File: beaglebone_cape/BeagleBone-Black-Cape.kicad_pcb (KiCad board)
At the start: 2 copper layers, 54.6 x 86.4 mm, 49 parts, among them J1 MC000052, J10 MOLEX_2031, J11 MOLEX_2021, J12 EBV-02-D, J2 MOLEX_2051, J3 MOLEX_2031, J4 MOLEX_2021, J5 MOLEX_2041, J6 MOLEX_2031, J7 MOLEX_2041, J8 MOLEX_2031, J9 MOLEX_2041, P1 BeagleBone_Black_Header, P2 BeagleBone_Black_Header, Q1 IRLB8721PBF, Q2 IRFML8244, U1 DIGIPOT_50K, U2 U_IC-HKB, U3 X_STEPPER, U4 Y_STEPPER, U5 Z_STEPPER

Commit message: finished layout of all PCBs
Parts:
- removed C1: 47nF, Capacitors_SMD:C_0805_HandSoldering
- removed C2, C6: 1uF, Capacitors_SMD:C_0805_HandSoldering
- removed C3: 0.1uF, Capacitors_SMD:C_0805_HandSoldering
- removed D5: 50V_1A, Diodes_SMD:D_SMA_Handsoldering
- removed J11, J4: MOLEX_2021, Connectors_Molex:Molex_KK-6410-02_02x2.54mm_Straight
- removed Q2: IRFML8244, TO_SOT_Packages_SMD:SOT-23
- removed R1, R2, R7: 10K, Resistors_SMD:R_0805_HandSoldering
- removed R3: 340K, Resistors_SMD:R_0805_HandSoldering
- removed TP1: TestPoint, Measurement_Points:Measurement_Point_Round-TH_Small
- removed U1: DIGIPOT_50K, Socket_BeagleBone_Black:TDFN-8-1EP
- removed U2: U_IC-HKB, Socket_BeagleBone_Black:ICHKB
- C4, C5, CP_1: footprint Capacitors_THT:CP_Radial_D6.3mm_P2.50mm -> Capacitor_THT:CP_Radial_D6.3mm_P2.50mm
- C7, C8, C9: footprint Capacitors_SMD:C_0805_HandSoldering -> Capacitor_SMD:C_0805_2012Metric_Pad1.15x1.40mm_HandSolder
- D1, D2, D3: footprint Diodes_SMD:D_SMA_Handsoldering -> Diode_SMD:D_SMA_Handsoldering
- D4: footprint TO_SOT_Packages_THT:TO-220-2_Vertical -> Package_TO_SOT_THT:TO-220-2_Vertical
- J10, J3, J6, J8: footprint Connectors_Molex:Molex_KK-6410-03_03x2.54mm_Straight -> Connector_Molex:Molex_KK-254_AE-6410-03A_1x03_P2.54mm_Vertical
- J12: footprint Connectors_Terminal_Blocks:TerminalBlock_bornier-2_P5.08mm -> TerminalBlock:TerminalBlock_bornier-2_P5.08mm
- J2: value MOLEX_2051 -> 10pinIDC; footprint Connectors_Molex:Molex_KK-6410-05_05x2.54mm_Straight -> Connector_IDC:IDC-Header_2x05_P2.54mm_Vertical
- J5, J7, J9: footprint Connectors_Molex:Molex_KK-6410-04_04x2.54mm_Straight -> Connector_Molex:Molex_KK-254_AE-6410-04A_1x04_P2.54mm_Vertical
- Q1: footprint TO_SOT_Packages_THT:TO-220-3_Vertical -> Package_TO_SOT_THT:TO-220-3_Vertical
- R4, R5, R6, R8: footprint Resistors_SMD:R_0805_HandSoldering -> Resistor_SMD:R_0805_2012Metric_Pad1.15x1.40mm_HandSolder
- moved J3 24.1 mm to (134.6, 65.0), turned to 90 degrees
- moved J2 17.5 mm to (124.3, 89.8), turned to 0 degrees
- moved J8 3.66 mm to (124.5, 80.8), turned to 90 degrees
- moved F2 2.07 mm to (152.1, 62.2)
- moved J6 1.11 mm to (134.6, 103.6)
- moved D4 0.94 mm to (159.9, 113.6)
- moved R5 0.42 mm to (129.3, 78.5), turned to 90 degrees
- moved Q1 0.28 mm to (150.5, 125.9)
- moved U5 0.23 mm to (148.6, 91.0)
- moved U3 0.18 mm to (132.7, 109.3)
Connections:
- J2 pad 1: +24V -> GND
- J2 pad 2: GND -> POLY_EN
- J2 pad 3: POLY_EN -> POLY_READY
- J2 pad 4: POLY_READY -> POLY_PWM
- J2 pad 5: POLY_PWM -> FAN_PWM
- J3 pad 1: +3V3 -> +12V
- J3 pad 2: PH_DIODE -> +5V
- P1 pad 11: Y_ENABLE -> Net-(P1-Pad11)
- P1 pad 18: Z_ENABLE -> Net-(P1-Pad18)
- P2 pad 12: X_ENABLE -> ENABLE
- U3 pad 1: X_ENABLE -> ENABLE
- U4 pad 1: Y_ENABLE -> ENABLE
- U5 pad 1: Z_ENABLE -> ENABLE
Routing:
- net GND: track 351.6 -> 205.6 mm
- net ENABLE: track 0.00 -> 137.4 mm
- net IC_HB_PWM2: track 111.6 -> 19.8 mm
- net FAN_PWM: track 33.0 -> 122.0 mm
- net X_ENABLE: track 69.3 -> 0.00 mm
- net IC_HB_PWM1: track 47.6 -> 14.1 mm
- net Z_ENABLE: track 33.0 -> 0.00 mm
- net +3V3: track 201.5 -> 169.8 mm
- net Net-(F2-Pad1): track 58.9 -> 29.7 mm
- net +5V: track 63.8 -> 85.7 mm
- net Y_ENABLE: track 13.6 -> 0.00 mm
- net POT_W: track 12.1 -> 0.00 mm
- net Net-(D5-Pad2): track 9.44 -> 0.00 mm
- net POLY_EN: track 20.7 -> 11.6 mm
- net SPIO_DI: track 122.9 -> 129.8 mm
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
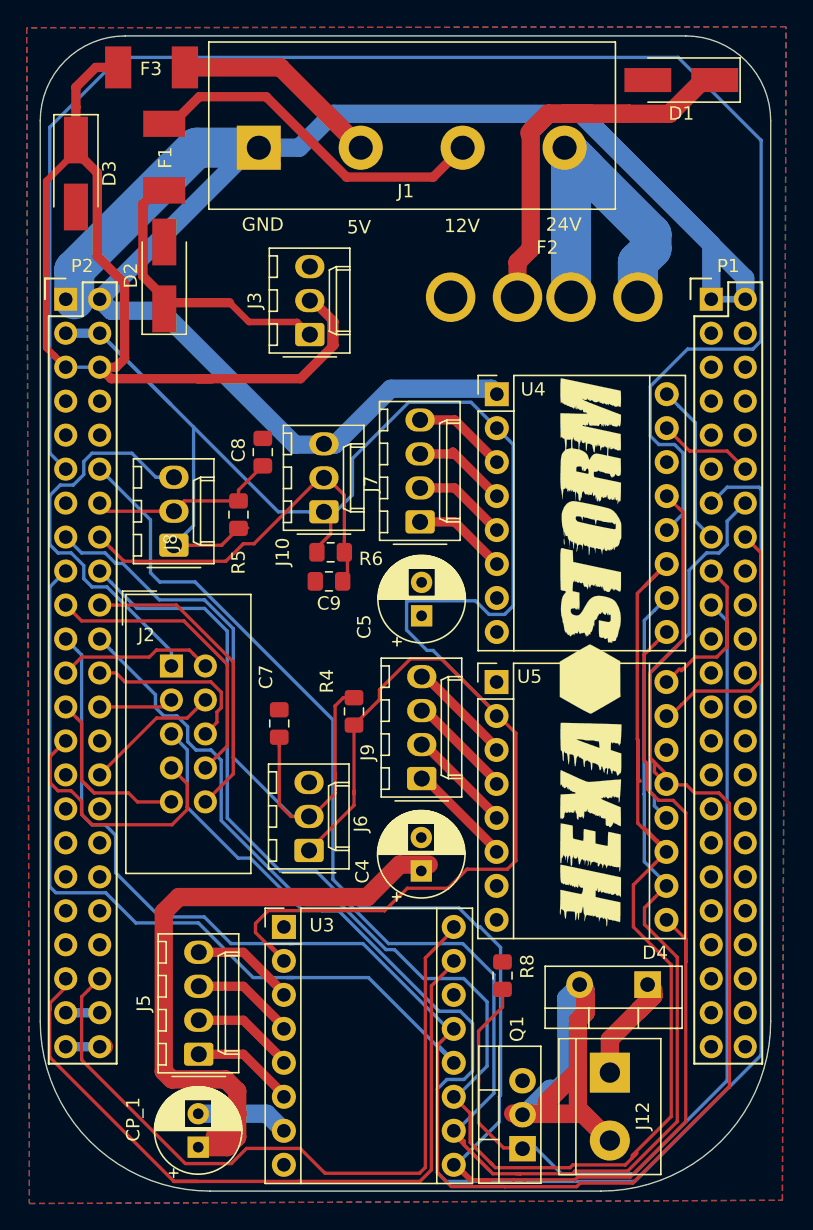
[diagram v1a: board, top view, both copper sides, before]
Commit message: fixed xpo pin connection
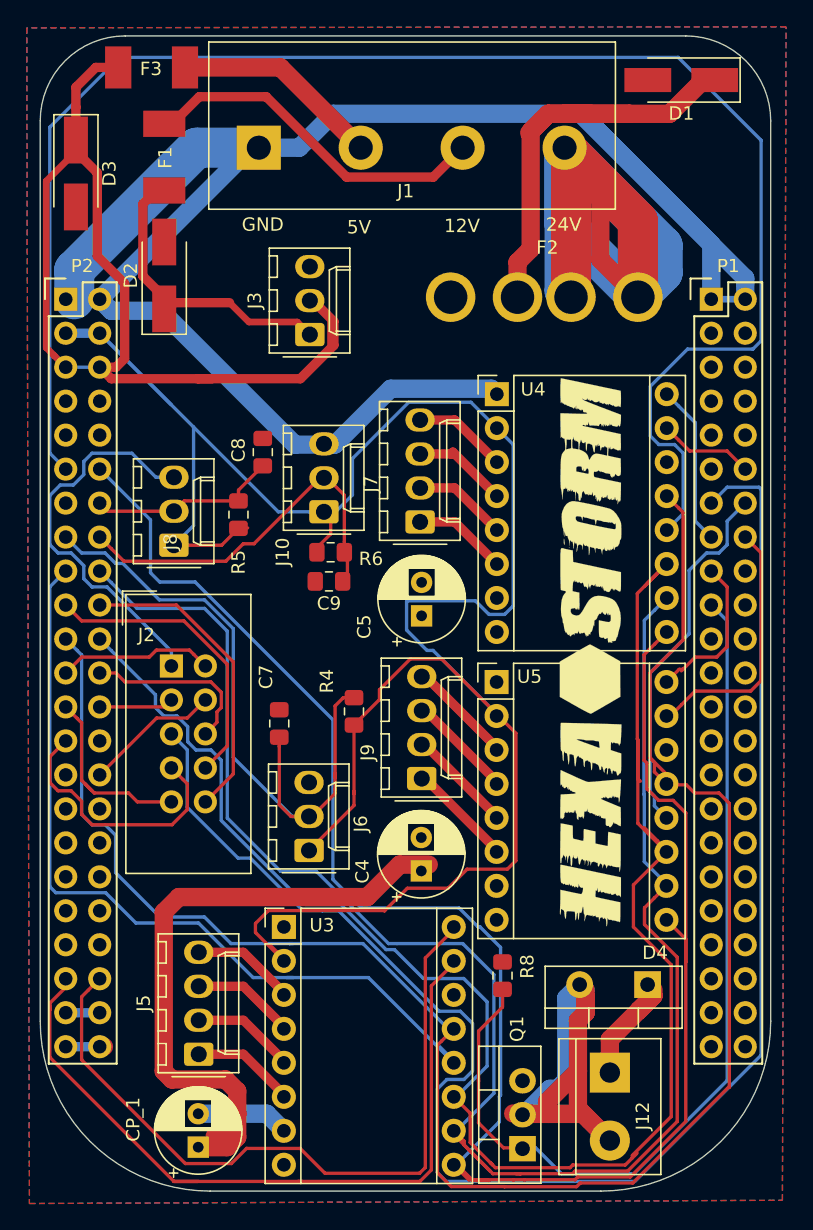
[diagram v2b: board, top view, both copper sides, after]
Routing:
- net Net-(F2-Pad1): track 29.7 -> 83.4 mm
- net X_PO: track 50.2 -> 51.5 mm
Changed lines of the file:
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@@
     (thickness 1.6)
     (drawings 8)
-    (tracks 638)
+    (tracks 649)
     (zones 0)
     (modules 34)
@@
     (0 F.Cu signal)
     (31 B.Cu signal)
-    (32 B.Adhes user hide)
-    (33 F.Adhes user hide)
+    (32 B.Adhes user)
+    (33 F.Adhes user)
     (34 B.Paste user)
     (35 F.Paste user)
@@
     (visible_elements 7FFFFFFF)
     (pcbplotparams
-      (layerselection 0x01030_ffffffff)
-      (usegerberextensions false)
+      (layerselection 0x010fc_ffffffff)
+      (usegerberextensions true)
       (usegerberattributes false)
       (usegerberadvancedattributes false)
@@
       (padsonsilk false)
       (subtractmaskfromsilk false)
-      (outputformat 4)
+      (outputformat 1)
       (mirror false)
       (drillshape 0)
       (scaleselection 1)
-      (outputdirectory "ratsnest"))
+      (outputdirectory "gerber/"))
   )
   (net 0 "")
@@
   (segment (start 137.922 91.94514) (end 137.922 91.84514) (width 0.25) (layer F.Cu) (net 92))
   (segment (start 132.334 95.484) (end 132.334 95.609) (width 0.25) (layer F.Cu) (net 92))
-  (segment (start 128.898623 96.642023) (end 133.22668 100.97008) (width 0.25) (layer B.Cu) (net 92))
-  (segment (start 128.898623 87.009101) (end 128.898623 96.642023) (width 0.25) (layer B.Cu) (net 92))
-  (segment (start 126.746 84.856478) (end 128.898623 87.009101) (width 0.25) (layer B.Cu) (net 92))
-  (segment (start 116.3701 80.1624) (end 117.558701 81.351001) (width 0.25) (layer B.Cu) (net 92))
-  (segment (start 117.558701 81.351001) (end 119.317831 81.351001) (width 0.25) (layer B.Cu) (net 92))
-  (segment (start 119.317831 81.351001) (end 120.098701 82.131871) (width 0.25) (layer B.Cu) (net 92))
-  (segment (start 120.098701 82.131871) (end 120.641871 82.131871) (width 0.25) (layer B.Cu) (net 92))
-  (segment (start 120.641871 82.131871) (end 123.366478 84.856478) (width 0.25) (layer B.Cu) (net 92))
-  (segment (start 123.366478 84.856478) (end 126.746 84.856478) (width 0.25) (layer B.Cu) (net 92))
   (segment (start 137.122 92.17014) (end 136.51 92.78214) (width 0.25) (layer F.Cu) (net 92))
   (segment (start 137.922 92.17014) (end 137.122 92.17014) (width 0.25) (layer F.Cu) (net 92))
@@
   (segment (start 134.56 101.05) (end 134.79 101.05) (width 0.25) (layer F.Cu) (net 92))
   (segment (start 136.51 99.03) (end 136.51 97.83) (width 0.25) (layer F.Cu) (net 92))
+  (segment (start 120.641871 82.131871) (end 120.098701 82.131871) (width 0.25) (layer B.Cu) (net 92))
+  (segment (start 133.3066 101.05) (end 128.898623 96.642023) (width 0.25) (layer B.Cu) (net 92))
+  (segment (start 134.56 101.05) (end 133.3066 101.05) (width 0.25) (layer B.Cu) (net 92))
+  (segment (start 117.558701 81.351001) (end 116.3701 80.1624) (width 0.25) (layer B.Cu) (net 92))
+  (segment (start 128.898623 96.642023) (end 128.898623 87.009101) (width 0.25) (layer B.Cu) (net 92))
+  (segment (start 128.898623 87.009101) (end 126.746 84.856478) (width 0.25) (layer B.Cu) (net 92))
+  (segment (start 119.317831 81.351001) (end 117.558701 81.351001) (width 0.25) (layer B.Cu) (net 92))
+  (segment (start 126.746 84.856478) (end 123.366478 84.856478) (width 0.25) (layer B.Cu) (net 92))
+  (segment (start 120.098701 82.131871) (end 119.317831 81.351001) (width 0.25) (layer B.Cu) (net 92))
+  (segment (start 123.366478 84.856478) (end 120.641871 82.131871) (width 0.25) (layer B.Cu) (net 92))
   (segment (start 153.66492 51.054) (end 155.025 52.41408) (width 3) (layer B.Cu) (net 98))
   (segment (start 155.162 52.55108) (end 153.66492 51.054) (width 3) (layer B.Cu) (net 98))
-  (segment (start 154.146 51.53508) (end 153.66492 51.054) (width 3) (layer B.Cu) (net 98))
-  (segment (start 154.146 62.23) (end 154.146 51.53508) (width 3) (layer B.Cu) (net 98))
-  (segment (start 153.66492 51.054) (end 160.162 57.55108) (width 3) (layer B.Cu) (net 98))
-  (segment (start 160.162 58.597705) (end 160.162 57.55108) (width 3) (layer B.Cu) (net 98))
-  (segment (start 159.146 59.613705) (end 160.162 58.597705) (width 3) (layer B.Cu) (net 98))
-  (segment (start 159.146 62.23) (end 159.146 59.613705) (width 3) (layer B.Cu) (net 98))
+  (segment (start 153.66492 61.74892) (end 154.146 62.23) (width 1.37) (layer F.Cu) (net 98))
+  (segment (start 155.314919 52.703999) (end 156.335999 52.703999) (width 1.37) (layer F.Cu) (net 98))
+  (segment (start 153.66492 51.054) (end 155.314919 52.703999) (width 1.37) (layer F.Cu) (net 98))
+  (segment (start 156.335999 59.419999) (end 159.146 62.23) (width 1.37) (layer F.Cu) (net 98))
+  (segment (start 156.335999 52.703999) (end 156.335999 59.419999) (width 1.37) (layer F.Cu) (net 98))
+  (segment (start 153.66492 61.74892) (end 154.146 62.23) (width 3) (layer B.Cu) (net 98))
+  (segment (start 153.66492 51.054) (end 153.66492 61.74892) (width 3) (layer B.Cu) (net 98))
+  (segment (start 153.66492 56.74892) (end 159.146 62.23) (width 3) (layer B.Cu) (net 98))
+  (segment (start 153.66492 51.054) (end 153.66492 56.74892) (width 3) (layer B.Cu) (net 98))
+  (segment (start 160.995999 60.380001) (end 159.146 62.23) (width 3) (layer B.Cu) (net 98))
+  (segment (start 160.995999 58.385079) (end 160.995999 60.380001) (width 3) (layer B.Cu) (net 98))
+  (segment (start 153.66492 51.054) (end 160.995999 58.385079) (width 3) (layer B.Cu) (net 98))
+  (segment (start 159.146 56.53508) (end 159.146 62.23) (width 3) (layer F.Cu) (net 98))
+  (segment (start 153.66492 51.054) (end 159.146 56.53508) (width 3) (layer F.Cu) (net 98))
+  (segment (start 154.146 51.53508) (end 153.66492 51.054) (width 3) (layer F.Cu) (net 98))
+  (segment (start 154.146 62.23) (end 154.146 51.53508) (width 3) (layer F.Cu) (net 98))
   (segment (start 145.743641 114.859229) (end 145.55724 114.859229) (width 0.25) (layer F.Cu) (net 101))
   (segment (start 154.440304 128.210022) (end 154.645303 128.005023) (width 0.25) (layer F.Cu) (net 104))
